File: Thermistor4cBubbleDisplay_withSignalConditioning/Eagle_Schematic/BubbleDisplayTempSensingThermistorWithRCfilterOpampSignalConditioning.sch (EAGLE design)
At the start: 29 parts, among them IC1 ATMEGA328-20P, U1 SN74HC595N, Y1 16MHz

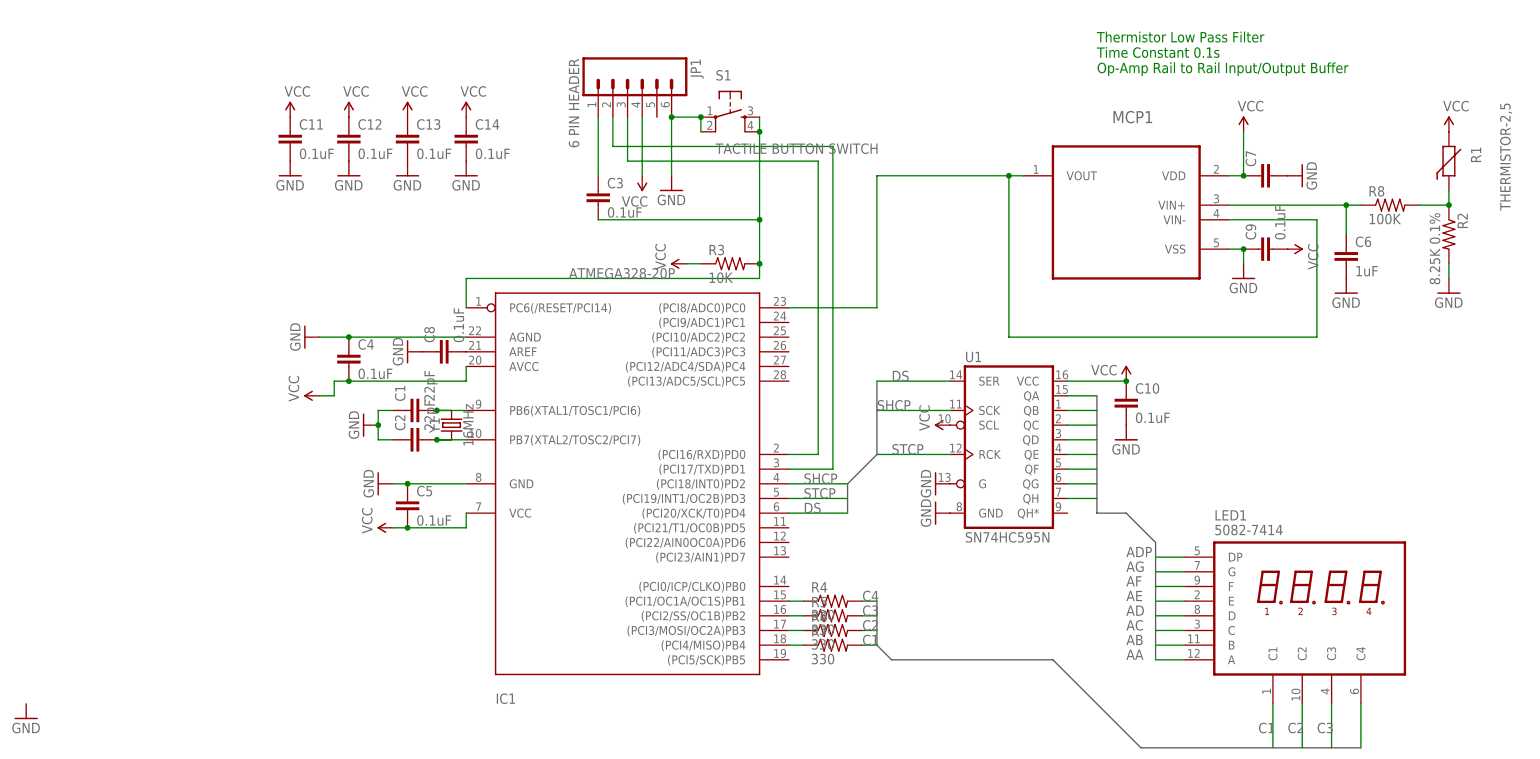
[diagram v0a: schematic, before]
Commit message: Updated schematics to reflect breadboard. This is to make it easier to resume work during/after semester and know 	what I'm up to and what needs to be done.
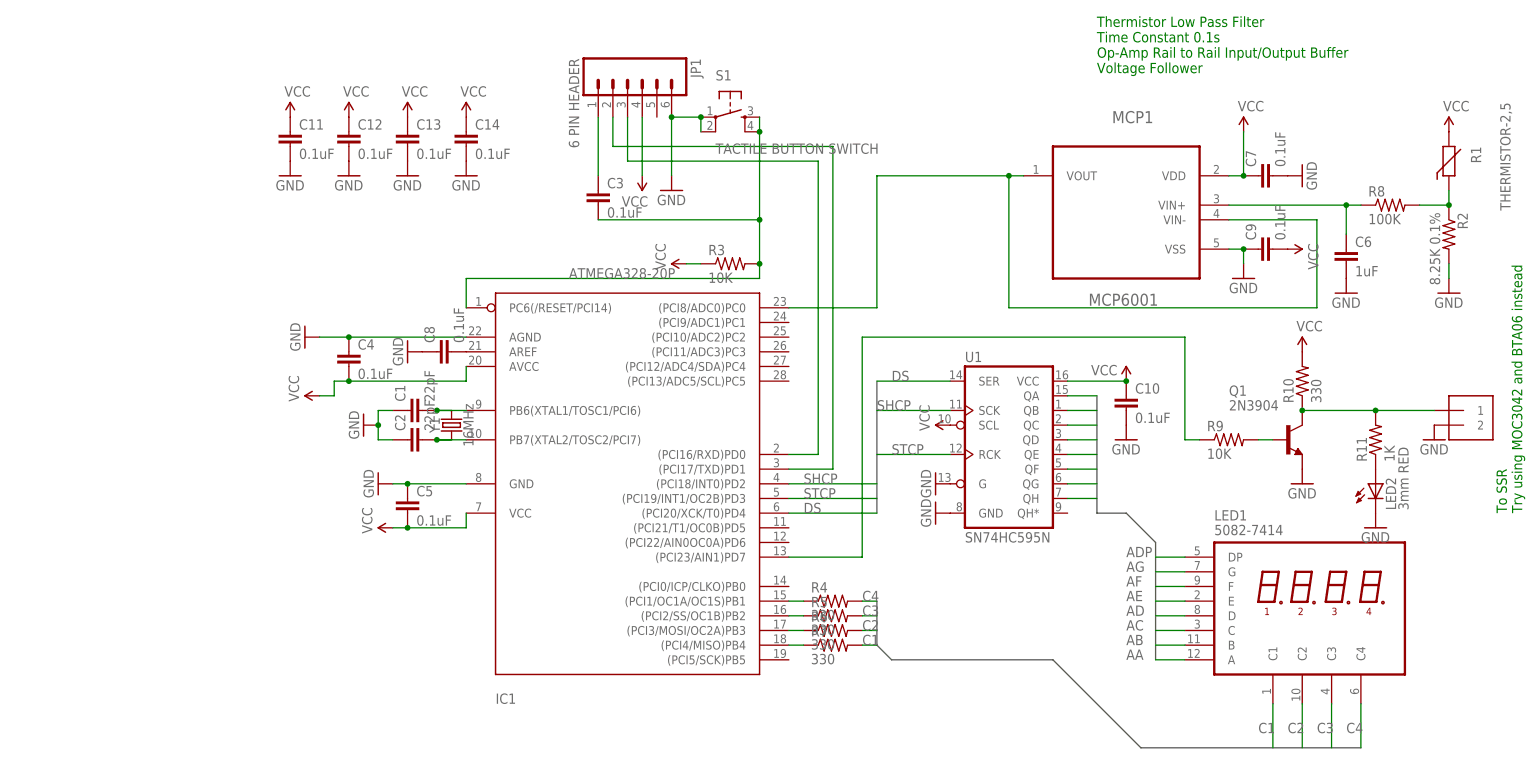
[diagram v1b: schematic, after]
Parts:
- added J1: 1X2-3.5MM, adafruit:1X2-3.5MM
- added LED2: 3mm RED, SparkFun-LED:LED3MM
- added Q1: 2N3904, Johnboiles:2N3904
- added R10: 330, SparkFun-Passives:RESISTORPTH-1/2W
- added R11: 1K, SparkFun-Passives:RESISTORPTH-1/2W
- added R9: 10K, SparkFun-Passives:RESISTORPTH-1/2W
- C7: value (none) -> 0.1uF
- MCP1: value (none) -> MCP6001
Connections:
- new net N$15: IC1.(PCI23/AIN1)PD7, R9.1
- new net N$16: Q1.B, R9.2
- new net N$17: J1.1, Q1.C, R10.1, R11.2
- new net N$18: LED2.A, R11.1
- net GND: now also J1.2, LED2.C, Q1.E
- net VCC: now also R10.2
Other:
- note added: "Thermistor Low Pass Filter Time Constant 0.1s Op-Amp Rail to Rail Input/Output Buffer Voltage Follower"
- note added: "To SSR Try using MOC3042 and BTA06 instead"
- note removed: "Thermistor Low Pass Filter Time Constant 0.1s Op-Amp Rail to Rail Input/Output Buffer"
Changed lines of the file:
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@@
 <part name="GND3" library="SparkFun-Aesthetics" deviceset="GND" device=""/>
 <part name="GND4" library="SparkFun-Aesthetics" deviceset="GND" device=""/>
-<part name="GND5" library="SparkFun-Aesthetics" deviceset="GND" device=""/>
 <part name="R1" library="varistor" deviceset="THERMISTOR" device="-2,5"/>
 <part name="R2" library="SparkFun-Passives" deviceset="RESISTOR" device="PTH-1/2W" value="8.25K 0.1%"/>
@@
 <part name="C5" library="SparkFun-Capacitors" deviceset="CAP" device="EZ" value="0.1uF"/>
 <part name="C6" library="SparkFun-Capacitors" deviceset="CAP" device="EZ" value="1uF"/>
-<part name="C7" library="SparkFun-Capacitors" deviceset="CAP" device="EZ"/>
+<part name="C7" library="SparkFun-Capacitors" deviceset="CAP" device="EZ" value="0.1uF"/>
 <part name="C8" library="SparkFun-Capacitors" deviceset="CAP" device="EZ" value="0.1uF"/>
 <part name="C9" library="SparkFun-Capacitors" deviceset="CAP" device="EZ" value="0.1uF"/>
@@
 <part name="R8" library="SparkFun-Passives" deviceset="RESISTOR" device="PTH-1/2W" value="100K"/>
 <part name="GND14" library="SparkFun-Aesthetics" deviceset="GND" device=""/>
-<part name="MCP1" library="Microchip_MCP6001R" deviceset="MCP6001R" device=""/>
+<part name="MCP1" library="Microchip_MCP6001R" deviceset="MCP6001R" device="" value="MCP6001"/>
 <part name="SUPPLY10" library="SparkFun-Aesthetics" deviceset="VCC" device=""/>
 <part name="GND15" library="SparkFun-Aesthetics" deviceset="GND" device=""/>
@@
 <part name="SUPPLY12" library="SparkFun-Aesthetics" deviceset="VCC" device=""/>
 <part name="SUPPLY13" library="SparkFun-Aesthetics" deviceset="VCC" device=""/>
+<part name="J1" library="adafruit" deviceset="1X2" device="-3.5MM"/>
+<part name="Q1" library="Johnboiles" deviceset="2N3904" device=""/>
+<part name="R9" library="SparkFun-Passives" deviceset="RESISTOR" device="PTH-1/2W" value="10K"/>
+<part name="GND5" library="SparkFun-Aesthetics" deviceset="GND" device=""/>
+<part name="R10" library="SparkFun-Passives" deviceset="RESISTOR" device="PTH-1/2W" value="330"/>
+<part name="SUPPLY14" library="SparkFun-Aesthetics" deviceset="VCC" device=""/>
+<part name="R11" library="SparkFun-Passives" deviceset="RESISTOR" device="PTH-1/2W" value="1K"/>
+<part name="GND18" library="SparkFun-Aesthetics" deviceset="GND" device=""/>
+<part name="LED2" library="SparkFun-LED" deviceset="LED" device="3MM" value="3mm RED"/>
+<part name="GND19" library="SparkFun-Aesthetics" deviceset="GND" device=""/>
 </parts>
 <sheets>
@@
 <text x="142.24" y="111.76" size="1.778" layer="91">Thermistor Low Pass Filter
 Time Constant 0.1s
-Op-Amp Rail to Rail Input/Output Buffer</text>
+Op-Amp Rail to Rail Input/Output Buffer
+Voltage Follower</text>
+<text x="215.9" y="35.56" size="1.778" layer="91" rot="R90">To SSR
+Try using MOC3042 and BTA06 instead</text>
 </plain>
 <instances>
@@
 <instance part="GND3" gate="1" x="68.58" y="91.44"/>
 <instance part="GND4" gate="1" x="17.78" y="40.64" rot="R270"/>
-<instance part="GND5" gate="1" x="-43.18" y="0"/>
 <instance part="R1" gate="G$1" x="203.2" y="96.52" smashed="yes" rot="R270">
 <attribute name="NAME" x="207.01" y="99.06" size="1.778" layer="95" rot="R270"/>
@@
 <instance part="SUPPLY12" gate="1" x="22.86" y="104.14"/>
 <instance part="SUPPLY13" gate="1" x="33.02" y="104.14"/>
+<instance part="J1" gate="G$1" x="205.74" y="50.8"/>
+<instance part="Q1" gate="G1" x="175.26" y="48.26"/>
+<instance part="R9" gate="G$1" x="165.1" y="48.26"/>
+<instance part="GND5" gate="1" x="177.8" y="40.64"/>
+<instance part="R10" gate="G$1" x="177.8" y="58.42" rot="R90"/>
+<instance part="SUPPLY14" gate="1" x="177.8" y="63.5"/>
+<instance part="R11" gate="G$1" x="190.5" y="48.26" rot="R90"/>
+<instance part="GND18" gate="1" x="190.5" y="33.02"/>
+<instance part="LED2" gate="G$1" x="190.5" y="40.64"/>
+<instance part="GND19" gate="1" x="200.66" y="48.26"/>
 </instances>
 <busses>
@@
 <bus name="SHCP,STCP,DS">
 <segment>
-<wire x1="104.14" y1="58.42" x2="104.14" y2="45.72" width="0.762" layer="92"/>
-<wire x1="104.14" y1="45.72" x2="99.06" y2="40.64" width="0.762" layer="92"/>
-<wire x1="99.06" y1="40.64" x2="99.06" y2="35.56" width="0.762" layer="92"/>
+<wire x1="104.14" y1="58.42" x2="104.14" y2="35.56" width="0.762" layer="92"/>
 </segment>
 </bus>
@@
 <pinref part="SUPPLY13" gate="1" pin="VCC"/>
 </segment>
+<segment>
+<pinref part="R10" gate="G$1" pin="2"/>
+<pinref part="SUPPLY14" gate="1" pin="VCC"/>
+</segment>
 </net>
 <net name="GND" class="0">
@@
 <pinref part="C14" gate="G$1" pin="2"/>
 <pinref part="GND8" gate="1" pin="GND"/>
+</segment>
+<segment>
+<pinref part="Q1" gate="G1" pin="E"/>
+<pinref part="GND5" gate="1" pin="GND"/>
+</segment>
+<segment>
+<pinref part="LED2" gate="G$1" pin="C"/>
+<pinref part="GND18" gate="1" pin="GND"/>
+</segment>
+<segment>
+<pinref part="J1" gate="G$1" pin="2"/>
+<pinref part="GND19" gate="1" pin="GND"/>
 </segment>
 </net>
@@
 <pinref part="LED1" gate="$1" pin="C4"/>
 <wire x1="187.96" y1="2.54" x2="187.96" y2="-5.08" width="0.1524" layer="91"/>
+<label x="185.42" y="-2.54" size="1.778" layer="95"/>
 </segment>
 </net>
@@
 <segment>
 <pinref part="IC1" gate="G$1" pin="(PCI18/INT0)PD2"/>
-<wire x1="88.9" y1="40.64" x2="99.06" y2="40.64" width="0.1524" layer="91"/>
+<wire x1="88.9" y1="40.64" x2="104.14" y2="40.64" width="0.1524" layer="91"/>
 <label x="91.44" y="40.64" size="1.778" layer="95"/>
 </segment>
@@
 <segment>
 <pinref part="IC1" gate="G$1" pin="(PCI19/INT1/OC2B)PD3"/>
-<wire x1="88.9" y1="38.1" x2="99.06" y2="38.1" width="0.1524" layer="91"/>
+<wire x1="88.9" y1="38.1" x2="104.14" y2="38.1" width="0.1524" layer="91"/>
 <label x="91.44" y="38.1" size="1.778" layer="95"/>
 </segment>
@@
 <segment>
 <pinref part="IC1" gate="G$1" pin="(PCI20/XCK/T0)PD4"/>
-<wire x1="88.9" y1="35.56" x2="99.06" y2="35.56" width="0.1524" layer="91"/>
+<wire x1="88.9" y1="35.56" x2="104.14" y2="35.56" width="0.1524" layer="91"/>
 <label x="91.44" y="35.56" size="1.778" layer="95"/>
 </segment>
@@
 <pinref part="MCP1" gate="A" pin="VIN-"/>
 <wire x1="165.1" y1="86.36" x2="180.34" y2="86.36" width="0.1524" layer="91"/>
-<wire x1="180.34" y1="86.36" x2="180.34" y2="66.04" width="0.1524" layer="91"/>
-<wire x1="180.34" y1="66.04" x2="127" y2="66.04" width="0.1524" layer="91"/>
-<wire x1="127" y1="66.04" x2="127" y2="93.98" width="0.1524" layer="91"/>
+<wire x1="180.34" y1="86.36" x2="180.34" y2="71.12" width="0.1524" layer="91"/>
+<wire x1="180.34" y1="71.12" x2="127" y2="71.12" width="0.1524" layer="91"/>
+<wire x1="127" y1="71.12" x2="127" y2="93.98" width="0.1524" layer="91"/>
 <junction x="127" y="93.98"/>
 </segment>
@@
 </segment>
 </net>
+<net name="N$15" class="0">
+<segment>
+<pinref part="IC1" gate="G$1" pin="(PCI23/AIN1)PD7"/>
+<wire x1="88.9" y1="27.94" x2="101.6" y2="27.94" width="0.1524" layer="91"/>
+<wire x1="101.6" y1="27.94" x2="101.6" y2="66.04" width="0.1524" layer="91"/>
+<wire x1="101.6" y1="66.04" x2="157.48" y2="66.04" width="0.1524" layer="91"/>
+<wire x1="157.48" y1="66.04" x2="157.48" y2="48.26" width="0.1524" layer="91"/>
+<pinref part="R9" gate="G$1" pin="1"/>
+<wire x1="157.48" y1="48.26" x2="160.02" y2="48.26" width="0.1524" layer="91"/>
+</segment>
+</net>
+<net name="N$16" class="0">
+<segment>
+<pinref part="R9" gate="G$1" pin="2"/>
+<pinref part="Q1" gate="G1" pin="B"/>
+<wire x1="170.18" y1="48.26" x2="172.72" y2="48.26" width="0.1524" layer="91"/>
+</segment>
+</net>
+<net name="N$17" class="0">
+<segment>
+<pinref part="Q1" gate="G1" pin="C"/>
+<pinref part="R10" gate="G$1" pin="1"/>
+<pinref part="J1" gate="G$1" pin="1"/>
+<wire x1="200.66" y1="53.34" x2="190.5" y2="53.34" width="0.1524" layer="91"/>
+<junction x="177.8" y="53.34"/>
+<pinref part="R11" gate="G$1" pin="2"/>
+<wire x1="190.5" y1="53.34" x2="177.8" y2="53.34" width="0.1524" layer="91"/>
+<junction x="190.5" y="53.34"/>
+</segment>
+</net>
+<net name="N$18" class="0">
+<segment>
+<pinref part="R11" gate="G$1" pin="1"/>
+<pinref part="LED2" gate="G$1" pin="A"/>
+</segment>
+</net>
